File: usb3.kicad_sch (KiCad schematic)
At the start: 44 parts, among them J4 USB3_A, J5 Conn_01x15_MountingPin, J6 USB_C_Receptacle_USB2.0_16P, Q1 BSS138, U10 TPD4E05U06QDQARQ1, U11 TPD4E05U06QDQARQ1, U5 AP22615A, U6 AP22615A, U7 TPD4E05U06QDQARQ1, U8 TPD4E05U06QDQARQ1, U9 TPD4E05U06QDQARQ1

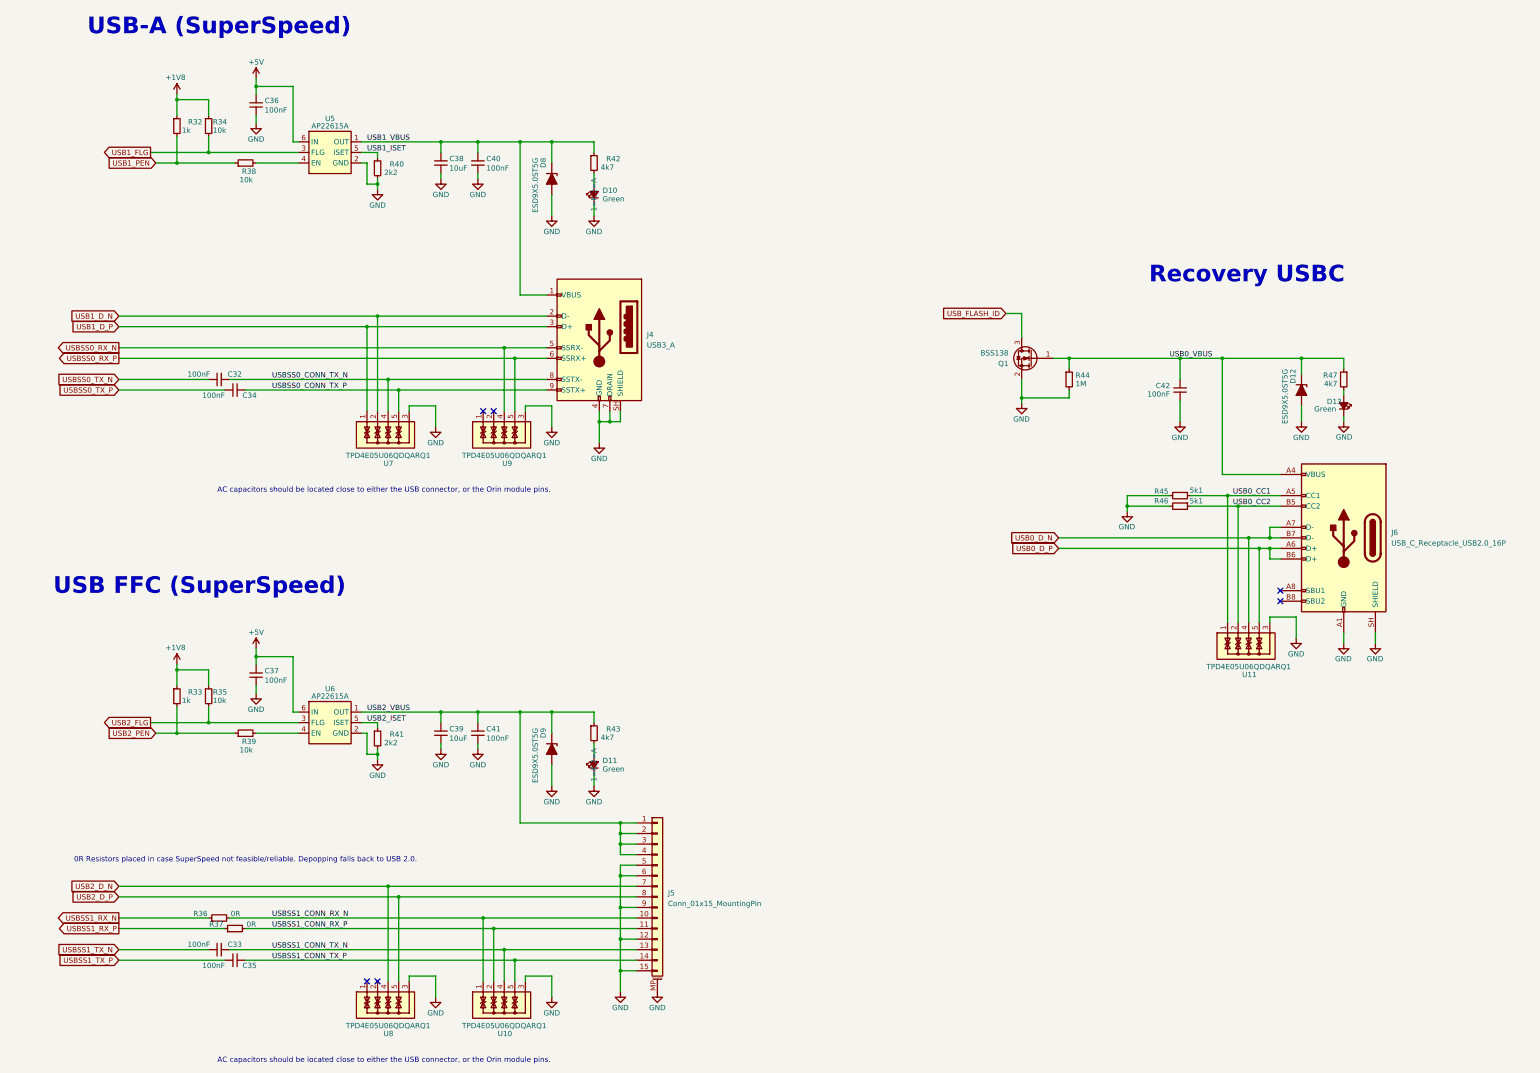
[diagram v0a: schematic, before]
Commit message: Replace current monitor w/ INA226 (addr = 0x42)
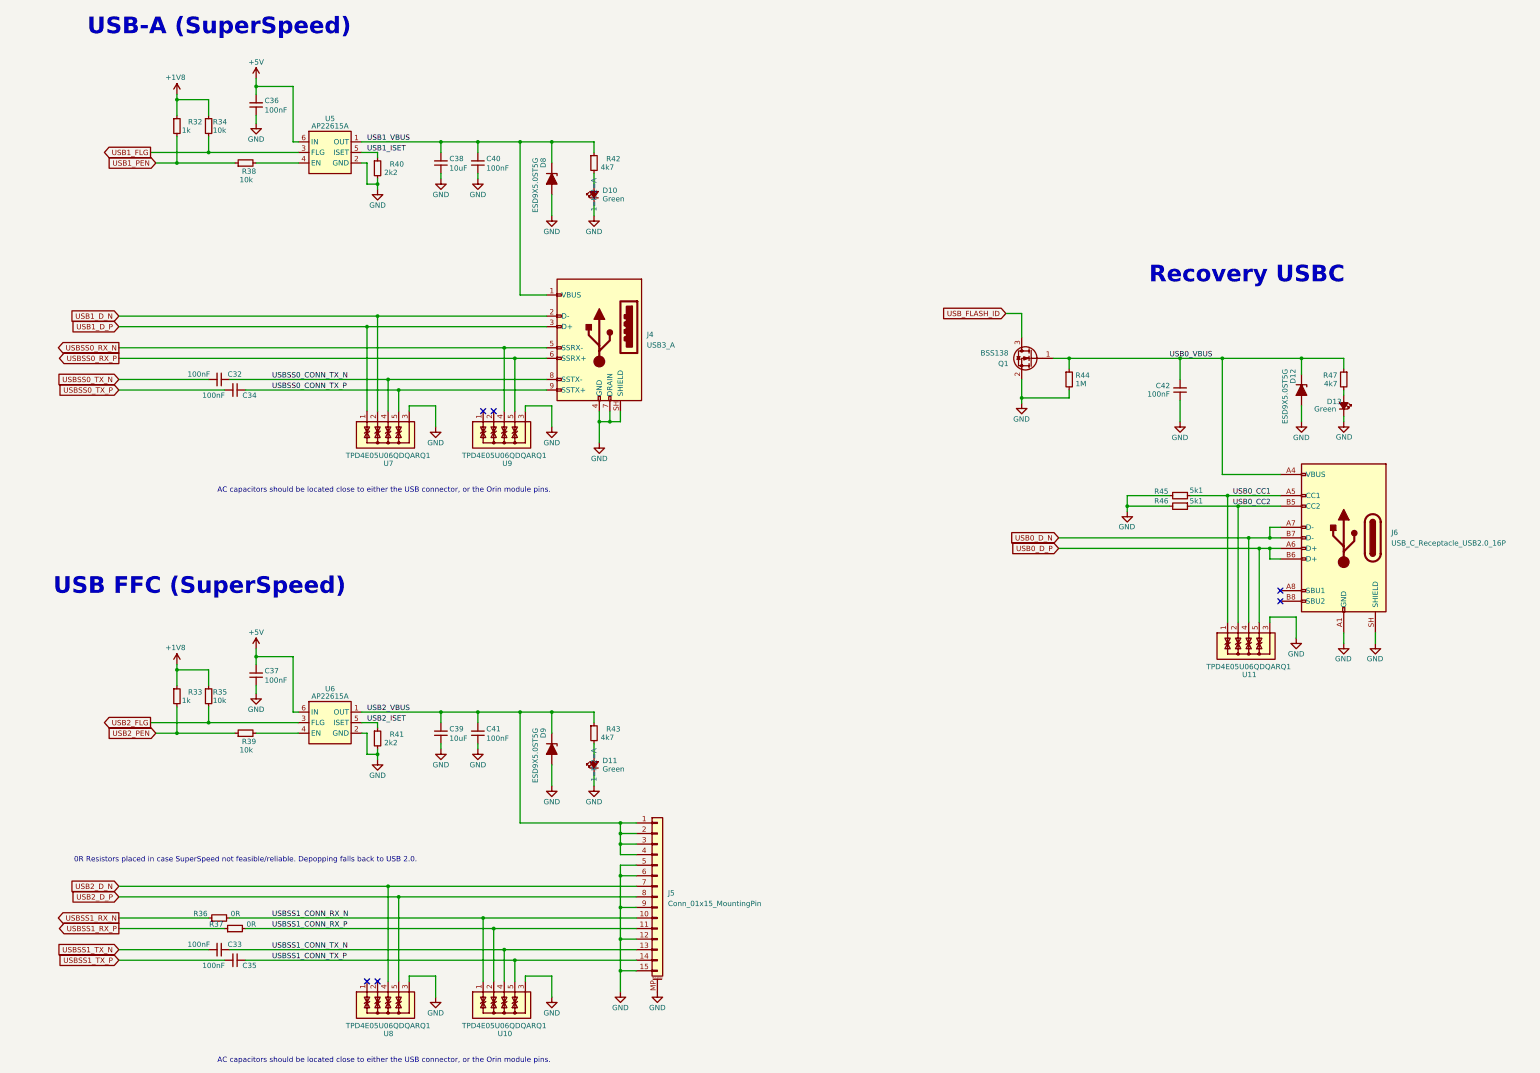
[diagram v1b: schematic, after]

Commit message: Final cleanup, production files
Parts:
- removed Q1: BSS138, Package_TO_SOT_SMD:SOT-23, symbol Transistor_FET:BSS138
- added Q1: 2N7002, Package_TO_SOT_SMD:SOT-23, symbol Transistor_FET:2N7002
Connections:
- net GND: now also Q1.2 (S)
- net USB0_VBUS: now also Q1.1 (G)
- net USB_FLASH_ID: now also Q1.3 (D)
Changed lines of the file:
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@@
 	)
 	(symbol
-		(lib_id "Transistor_FET:BSS138")
-		(at 274.32 106.68 0)
-		(mirror y)
-		(unit 1)
-		(body_style 1)
-		(exclude_from_sim no)
-		(in_bom yes)
-		(on_board yes)
-		(in_pos_files yes)
-		(dnp no)
-		(property "Reference" "Q1"
-			(at 268.605 107.9501 0)
-			(show_name no)
-			(do_not_autoplace no)
-			(effects
-				(font
-					(size 1.27 1.27)
-				)
-				(justify left)
-			)
-		)
-		(property "Value" "BSS138"
-			(at 268.605 105.4101 0)
-			(show_name no)
-			(do_not_autoplace no)
-			(effects
-				(font
-					(size 1.27 1.27)
-				)
-				(justify left)
-			)
-		)
-		(property "Footprint" "Package_TO_SOT_SMD:SOT-23"
-			(at 269.24 108.585 0)
-			(hide yes)
-			(show_name no)
-			(do_not_autoplace no)
-			(effects
-				(font
-					(size 1.27 1.27)
-					(italic yes)
-				)
-				(justify left)
-			)
-		)
-		(property "Datasheet" "https://www.onsemi.com/pub/Collateral/BSS138-D.PDF"
-			(at 269.24 110.49 0)
-			(hide yes)
-			(show_name no)
-			(do_not_autoplace no)
-			(effects
-				(font
-					(size 1.27 1.27)
-				)
-				(justify left)
-			)
-		)
-		(property "Description" "50V Vds, 0.22A Id, N-Channel MOSFET, SOT-23"
-			(at 274.32 106.68 0)
-			(hide yes)
-			(show_name no)
-			(do_not_autoplace no)
-			(effects
-				(font
-					(size 1.27 1.27)
-				)
-			)
-		)
-		(pin "2"
-		)
-		(pin "3"
-		)
-		(pin "1"
-		)
-		(instances
-			(project "jetson-orin-baseboard"
-				(path "/4b393452-b11e-416e-bc83-918ae3cab2f1/48dc7bcf-c3fe-4bb4-a045-e4bc8a9ae6bd"
-					(reference "Q1")
-					(unit 1)
-				)
-			)
-		)
-	)
-	(symbol
 		(lib_id "Device:D_Zener_Filled")
 		(at 158.75 200.66 270)
@@
 					(unit 1)
 				)
+			)
+		)
+	)
+	(symbol
+		(lib_id "Transistor_FET:2N7002")
+		(at 274.32 106.68 0)
+		(mirror y)
+		(unit 1)
+		(body_style 1)
+		(exclude_from_sim no)
+		(in_bom yes)
+		(on_board yes)
+		(in_pos_files yes)
+		(dnp no)
+		(fields_autoplaced yes)
+		(property "Reference" "Q1"
+			(at 268.605 105.4099 0)
+			(show_name no)
+			(do_not_autoplace no)
+			(effects
+				(font
+					(size 1.27 1.27)
+				)
+				(justify left)
+			)
+		)
+		(property "Value" "2N7002"
+			(at 268.605 107.9499 0)
+			(show_name no)
+			(do_not_autoplace no)
+			(effects
+				(font
+					(size 1.27 1.27)
+				)
+				(justify left)
+			)
+		)
+		(property "Footprint" "Package_TO_SOT_SMD:SOT-23"
+			(at 269.24 108.585 0)
+			(hide yes)
+			(show_name no)
+			(do_not_autoplace no)
+			(effects
+				(font
+					(size 1.27 1.27)
+					(italic yes)
+				)
+				(justify left)
+			)
+		)
+		(property "Datasheet" "https://www.onsemi.com/pub/Collateral/NDS7002A-D.PDF"
+			(at 269.24 110.49 0)
+			(hide yes)
+			(show_name no)
+			(do_not_autoplace no)
+			(effects
+				(font
+					(size 1.27 1.27)
+				)
+				(justify left)
+			)
+		)
+		(property "Description" "0.115A Id, 60V Vds, N-Channel MOSFET, SOT-23"
+			(at 274.32 106.68 0)
+			(hide yes)
+			(show_name no)
+			(do_not_autoplace no)
+			(effects
+				(font
+					(size 1.27 1.27)
+				)
+			)
+		)
+		(pin "3"
+		)
+		(pin "1"
+		)
+		(pin "2"
+		)
+		(instances
+			(project "jetson-orin-baseboard"
+				(path "/4b393452-b11e-416e-bc83-918ae3cab2f1/48dc7bcf-c3fe-4bb4-a045-e4bc8a9ae6bd"
+					(reference "Q1")
+					(unit 1)
+				)

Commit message: Add 3D models
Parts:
- J4: footprint Connector_USB:USB3_A_Molex_48393-001 -> Argus-Connectors:USB-A_3.0_GSB311131HR
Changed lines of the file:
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@@
 			)
 		)
-		(property "Footprint" "Connector_USB:USB3_A_Molex_48393-001"
+		(property "Footprint" "Argus-Connectors:USB-A_3.0_GSB311131HR"
 			(at 166.37 99.06 0)
 			(hide yes)

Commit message: Final BOM changes, gerbers
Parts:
- C32, C33, C34, C35: LCSC (none) -> C307331
- C36, C37, C40, C41, C42: LCSC (none) -> C14663
- C38, C39: LCSC (none) -> C96446
- D10, D11, D13: LCSC (none) -> C12065
- D12, D8, D9: LCSC (none) -> C87910
- J4: LCSC (none) -> C473057
- J6: LCSC (none) -> C3020560
- Q1: LCSC (none) -> C8545
- R32, R33: LCSC (none) -> C21190
- R34, R35, R38, R39: LCSC (none) -> C25804
- R36, R37: LCSC (none) -> C17168
- R40, R41: LCSC (none) -> C4190
- R42, R43, R47: LCSC (none) -> C23162
- R44: LCSC (none) -> C22935
- R45, R46: LCSC (none) -> C23186
- U10, U11, U7, U8, U9: LCSC (none) -> C81353
- U5, U6: LCSC (none) -> C2680357
